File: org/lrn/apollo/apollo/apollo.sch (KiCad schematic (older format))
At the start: 69 parts, among them J10 Conn_01x01_Male, J11 Conn_01x01_Male, J12 Conn_01x01_Male, J13 Conn_01x01_Male, J17 Conn_01x01_Male, J18 Conn_01x01_Male, J4 Conn_01x01_Male, J6 Conn_01x01_Male, J7 Conn_01x01_Male, J8 Conn_01x01_Male, J9 Conn_01x01_Male, Q1 PN2222A, Q2 PN2222A, Q3 PN2222A, Q4 PN2222A, Q5 PN2222A, Q6 PN2222A, U1 74HC595, U2 5461AS-1, U3 74HC595, U4 ATmega168P-20PU

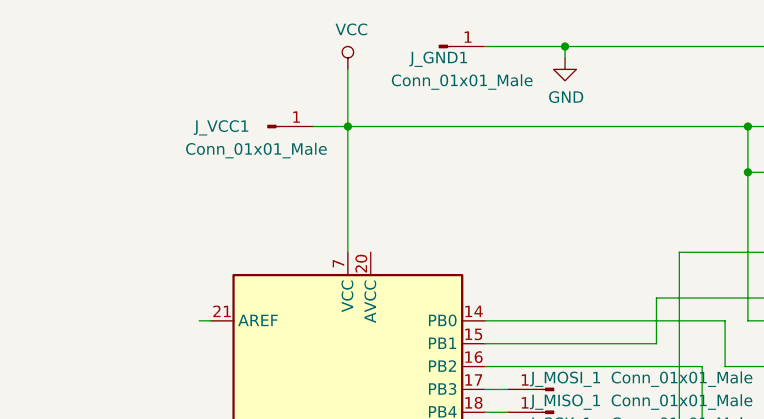
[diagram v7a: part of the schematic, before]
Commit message: apollo:scheme micro usb connector for vcc and gnd
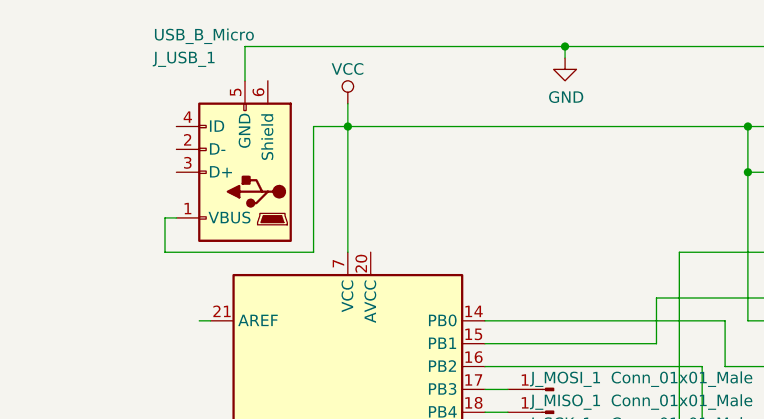
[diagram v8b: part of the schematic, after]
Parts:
- removed J_GND1, J_VCC1: Conn_01x01_Male, Connector_Pin:Pin_D0.7mm_L6.5mm_W1.8mm_FlatFork, symbol Connector:Conn_01x01_Male
- added J_USB_1: USB_B_Micro, Connector_USB:USB_Micro-AB_Molex_47590-0001, symbol Connector:USB_B_Micro
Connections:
- net GND: now also J_USB_1.5 (GND)
- net VCC: now also J_USB_1.1 (VBUS)
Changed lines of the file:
@@
 	7050 3800 7050 3950
-$Comp
-L Connector:Conn_01x01_Male J_VCC1
-U 1 1 5F4B5699
-P 1000 950
-F 0 "J_VCC1" H 800 950 50  0000 C CNN
-F 1 "Conn_01x01_Male" H 950 850 50  0000 C CNN
-F 2 "Connector_Pin:Pin_D0.7mm_L6.5mm_W1.8mm_FlatFork" H 1000 950 50  0001 C CNN
-F 3 "~" H 1000 950 50  0001 C CNN
-	1    1000 950
-	1    0    0    -1
-$EndComp
-$Comp
-L Connector:Conn_01x01_Male J_GND1
-U 1 1 5F4C3172
-P 1750 600
-F 0 "J_GND1" H 1750 550 50  0000 C CNN
-F 1 "Conn_01x01_Male" H 1850 450 50  0000 C CNN
-F 2 "Connector_Pin:Pin_D0.7mm_L6.5mm_W1.8mm_FlatFork" H 1750 600 50  0001 C CNN
-F 3 "~" H 1750 600 50  0001 C CNN
-	1    1750 600
-	1    0    0    -1
-$EndComp
 $Comp
 L Device:R Rb1
@@
 L power:VCC #PWR0101
 U 1 1 5F60A86A
-P 1350 700
-F 0 "#PWR0101" H 1350 550 50  0001 C CNN
-F 1 "VCC" H 1367 873 50  0000 C CNN
-F 2 "" H 1350 700 50  0001 C CNN
-F 3 "" H 1350 700 50  0001 C CNN
-	1    1350 700
+P 1350 850
+F 0 "#PWR0101" H 1350 700 50  0001 C CNN
+F 1 "VCC" H 1350 1000 50  0000 C CNN
+F 2 "" H 1350 850 50  0001 C CNN
+F 3 "" H 1350 850 50  0001 C CNN
+	1    1350 850
 	1    0    0    -1
 $EndComp
@@
 Wire Wire Line
 	1200 950  1350 950
-Wire Wire Line
-	1350 700  1350 950
 Connection ~ 1350 950
 Connection ~ 6500 3800
@@
 Connection ~ 4600 600
 Wire Wire Line
-	1950 600  2300 600
-Wire Wire Line
 	2300 650  2300 600
 Connection ~ 2300 600
@@
 Wire Wire Line
 	4100 2200 4100 5800
+$Comp
+L Connector:USB_B_Micro J_USB_1
+U 1 1 5F8532C6
+P 900 1150
+F 0 "J_USB_1" H 1300 650 50  0000 R CNN
+F 1 "USB_B_Micro" H 1300 550 50  0000 R CNN
+F 2 "Connector_USB:USB_Micro-AB_Molex_47590-0001" H 1050 1100 50  0001 C CNN
+F 3 "~" H 1050 1100 50  0001 C CNN
+	1    900  1150
+	-1   0    0    1
+$EndComp
+Wire Wire Line
+	900  750  900  600
+Wire Wire Line
+	900  600  2300 600
+Wire Wire Line
+	600  1350 550  1350
+Wire Wire Line
+	550  1350 550  1500
+Wire Wire Line
+	550  1500 1200 1500
+Wire Wire Line
+	1200 1500 1200 950
+Wire Wire Line
+	1350 850  1350 950
 $EndSCHEMATC
